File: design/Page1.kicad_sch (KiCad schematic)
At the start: 25 parts, among them J3 Jack-DC, J4 Conn_01x04_Male, J8 power in, Q12 DMN26D0UT-7, Q3 DMN26D0UT-7, Q4 DMN26D0UT-7, U5 TLV62569DDC, U6 TLV70018DCKT

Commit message: updated, its functional, but needs routing finished. tweeks from Bornhack 2026 to be added. :)
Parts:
- removed C14: 6.8pF, Capacitor_SMD:C_0402_1005Metric, symbol Device:C
- removed C16, C17: 10uF, Capacitor_SMD:C_0603_1608Metric, symbol Device:C
- removed C9: 4.7uF, Capacitor_SMD:C_0402_1005Metric, symbol Device:C
- removed L1: 2.2uH, Inductor_SMD:L_Bourns_SRP7028A_7.3x6.6mm, symbol Device:L
- removed R10: 1k, Resistor_SMD:R_0402_1005Metric, symbol Device:R
- removed R11: 12k, Resistor_SMD:R_0402_1005Metric, symbol Device:R
- removed R6: 100R, Resistor_SMD:R_0402_1005Metric, symbol Device:R
- removed R7: 4.7k, Resistor_SMD:R_0402_1005Metric, symbol Device:R
- removed U5: TLV62569DDC, Package_TO_SOT_SMD:SOT-23-6, symbol Regulator_Switching:TLV62569DDC
- added C10, C20: 10uF, Capacitor_SMD:C_0805_2012Metric_Pad1.18x1.45mm_HandSolder, symbol Device:C
- added C21: 1uF, Capacitor_SMD:C_0805_2012Metric_Pad1.18x1.45mm_HandSolder, symbol Device:C
- added C30, C31, C61: 10uF, Capacitor_SMD:C_0805_2012Metric, symbol Device:C_Polarized_Small
- added JP2: SolderJumper_3_Bridged12, Jumper:SolderJumper-3_P1.3mm_Bridged2Bar12_RoundedPad1.0x1.5mm, symbol Jumper:SolderJumper_3_Bridged12
- added JP3: SolderJumper_2_Bridged, Jumper:SolderJumper-2_P1.3mm_Bridged2Bar_RoundedPad1.0x1.5mm, symbol Jumper:SolderJumper_2_Bridged
- added R17: 12k, Resistor_SMD:R_0805_2012Metric_Pad1.20x1.40mm_HandSolder, symbol Device:R
- added U3: AMS1117-3.3, Package_TO_SOT_SMD:SOT-223-3_TabPin2, symbol Regulator_Linear:AMS1117-3.3
- added U4: AMS1117-1.8, Package_TO_SOT_SMD:SOT-223-3_TabPin2, symbol Regulator_Linear:AMS1117-1.8
- added U7: AP2112K-3.3, Package_TO_SOT_SMD:SOT-23-5, symbol Regulator_Linear:AP2112K-3.3
- C11, C12: footprint Capacitor_SMD:C_0402_1005Metric -> Capacitor_SMD:C_0805_2012Metric_Pad1.18x1.45mm_HandSolder
- C15: footprint Capacitor_SMD:C_0402_1005Metric -> Capacitor_SMD:C_0805_2012Metric_Pad1.18x1.45mm_HandSolder; Manufacturer (none) -> C1525
- J8: now not fitted
- R12, R19: value 100k -> 12k; footprint Resistor_SMD:R_0402_1005Metric -> Resistor_SMD:R_0805_2012Metric_Pad1.20x1.40mm_HandSolder; Manufacturer C25741 -> C25744; Package 0402 -> (none)
- R14: footprint Resistor_SMD:R_0402_1005Metric -> Resistor_SMD:R_0805_2012Metric_Pad1.20x1.40mm_HandSolder
- R16: footprint Resistor_SMD:R_0402_1005Metric -> Resistor_SMD:R_0805_2012Metric_Pad1.20x1.40mm_HandSolder; Manufacturer (none) -> C25905
- R20: footprint Resistor_SMD:R_0402_1005Metric -> Resistor_SMD:R_0805_2012Metric_Pad1.20x1.40mm_HandSolder; Package 0402 -> (none); Tolerance (none) -> 5%
- U6: now not fitted; now left out of the parts list
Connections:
- net +1V8: now also C61.1, JP2.1 (A), U4.2 (VO)
- net +3.3V: now also C20.1, C21.1, C31.1, U3.2 (VO), U4.3 (VI), U7.5 (VOUT)
- net +5V: now also C10.1, C30.1, JP2.3 (B), R17.1, U3.3 (VI), U7.1 (VIN); no longer R20.1
- net FAN_TACH_IN: now also JP3.2 (B)
- net GND: now also C10.2, C20.2, C21.2, C30.2, C31.2, C61.2, U3.1 (GND), U4.1 (GND), U7.2 (GND)
- net GPIO08: now also JP3.1 (A)
- new net: JP2.2 (C), R20.1
- new net: R17.2, U7.3 (EN)
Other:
- note added: "DNP for MPV"
- note added: "consider removing 3.3v and 1.8v voltage rale, only used fo rpullups."
- note added: "tie hi or replace with regulator"
- note removed: "0.588V"
- note removed: "0.612V"
- note removed: "0.6V"
- note removed: "FISH : consider replacing with more common footprint. and yes pin 5 is needed. unless ..... ask Daniel."
- note removed: "Vfb"
- note removed: "max"
- note removed: "min"
- note removed: "no stuff this capacitor"
- note removed: "nom"
- moved on the sheet: C11, C12, C15

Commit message: updated little details.
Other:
- note added: "DNP for MPV (not realy needed)"
- note removed: "DNP for MPV"
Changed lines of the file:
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@@
-		)
-	)
-	(text "DNP \nfor MPV"
-		(exclude_from_sim no)
-		(at 97.282 153.162 0)
-		(effects
-			(font
-				(size 0.9906 0.9906)
-			)
 		)
 	)
@@
 			)
 			(justify left bottom)
+		)
+	)
+	(text "DNP \nfor MPV\n(not realy needed)"
+		(exclude_from_sim no)
+		(at 97.282 153.924 0)
+		(effects
+			(font
+				(size 0.9906 0.9906)
+			)
 		)
 	)
@@
 		)
 	)
-	(text "DNP \nfor MPV"
+	(text "DNP \nfor MPV\n(not realy needed)"
 		(exclude_from_sim no)
 		(at 151.638 146.812 0)

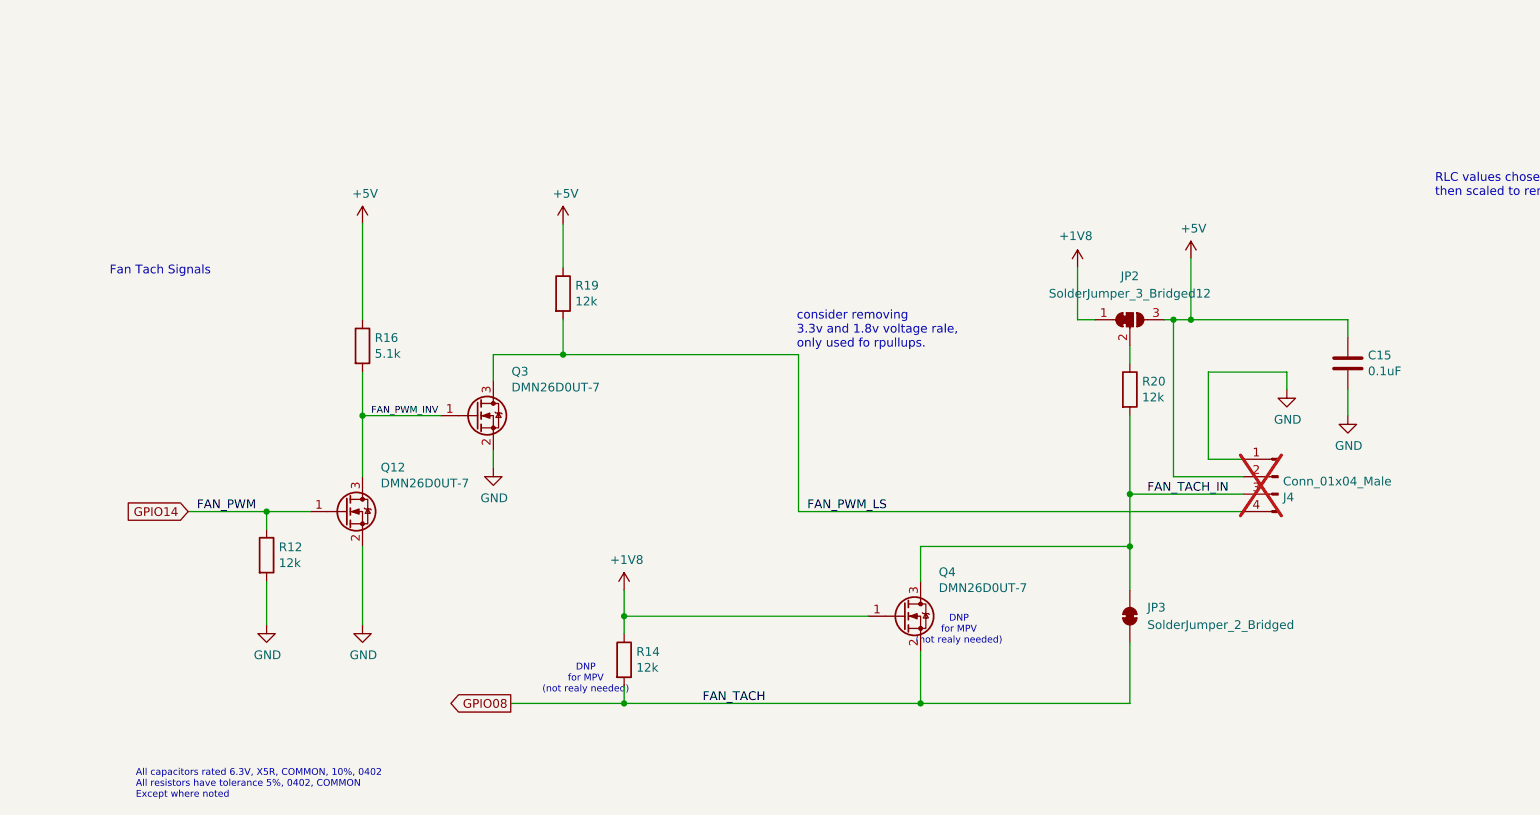
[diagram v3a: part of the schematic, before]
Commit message: added a 3 pin fan header PWM controlled of course.
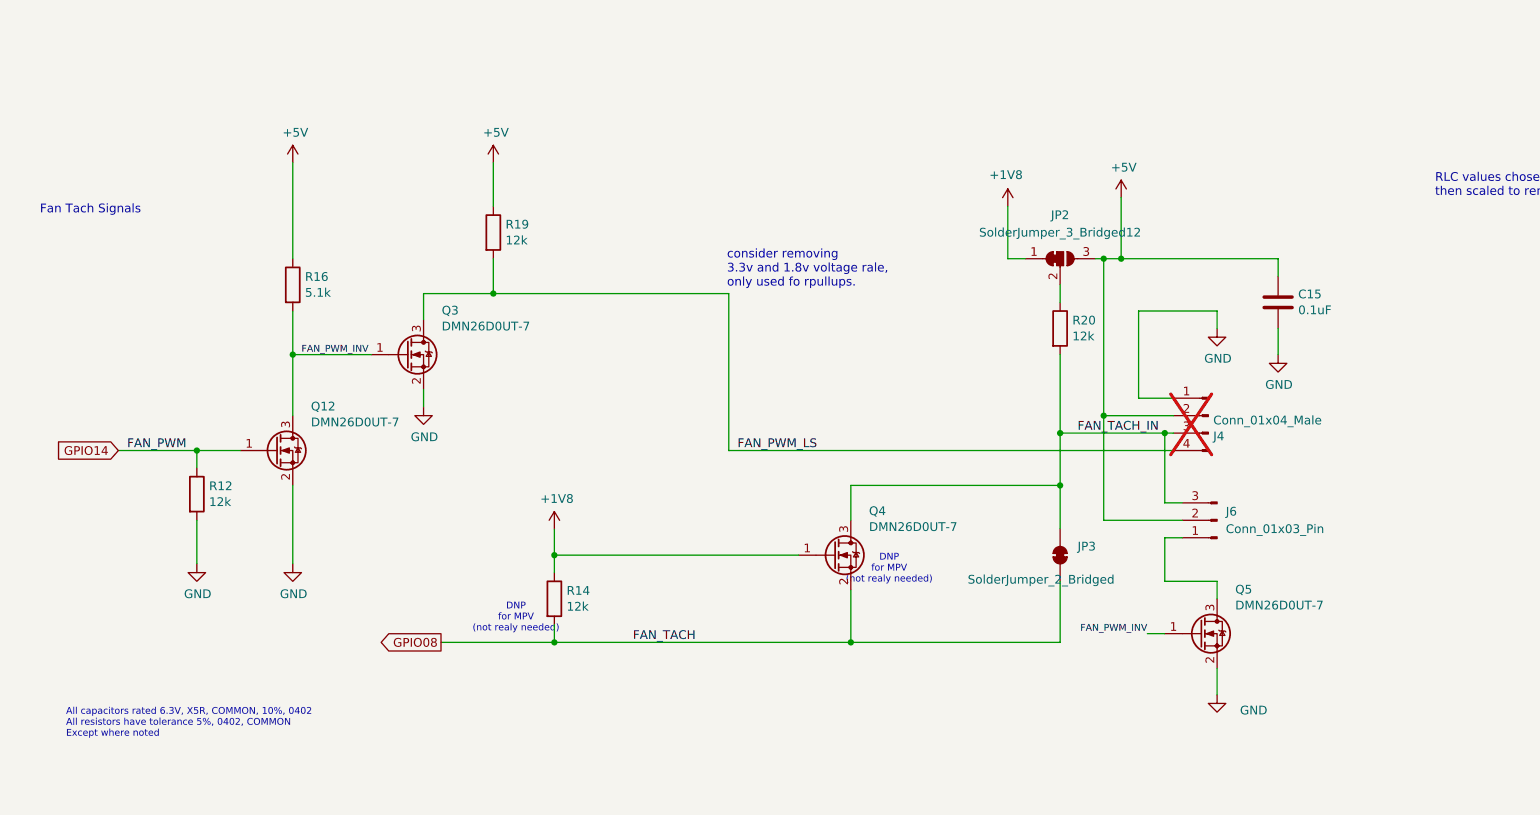
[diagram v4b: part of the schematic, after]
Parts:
- added J6: Conn_01x03_Pin, Connector_PinHeader_2.54mm:PinHeader_1x03_P2.54mm_Vertical, symbol Connector:Conn_01x03_Pin
- added Q5: DMN26D0UT-7, Package_TO_SOT_SMD:SOT-523, symbol Transistor_FET:2N7002
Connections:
- net +5V: now also J6.2 (Pin_2)
- net FAN_PWM_INV: now also Q5.1 (G)
- net FAN_TACH_IN: now also J6.3 (Pin_3)
- net GND: now also Q5.2 (S)
- new net: J6.1 (Pin_1), Q5.3 (D)
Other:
- moved on the sheet: C15, J4, JP2, JP3, Q12, Q3, Q4, R12, R14, R16, R19, R20
